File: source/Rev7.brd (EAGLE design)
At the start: 17.4 x 19 mm, 8 parts

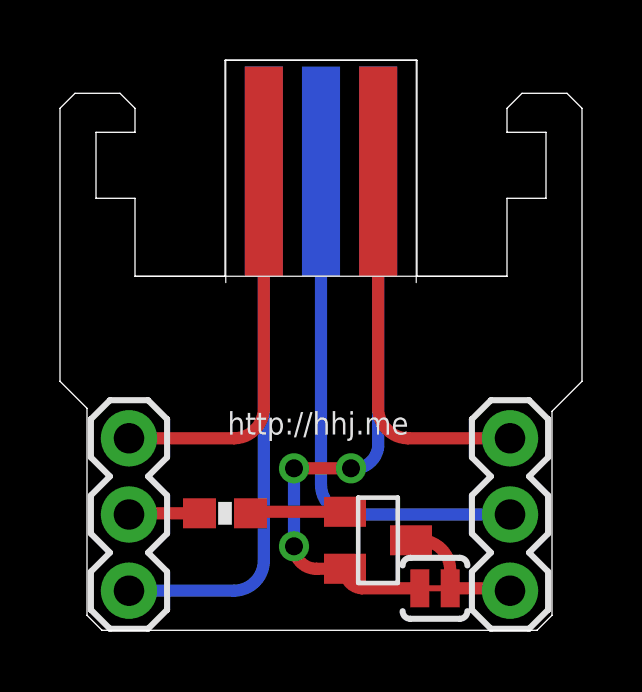
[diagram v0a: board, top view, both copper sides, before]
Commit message: Updated Rev7: down to 1 via and much better signal layout. Pin layout has changed
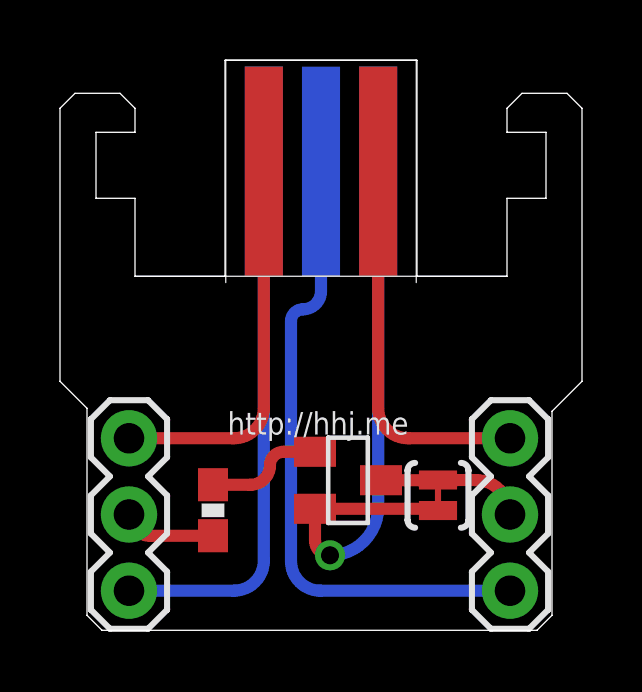
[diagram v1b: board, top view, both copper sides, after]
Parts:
- moved SJ1 3.10 mm to (12.1, 4.50), turned to 90 degrees
- moved Q1 2.24 mm to (9.10, 5.00)
- moved R1 0.41 mm to (4.60, 4.00), turned to 90 degrees
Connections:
- removed net PRES: JP2.2, U$1.PRESENCE
- new net N$2: JP2.3, U$1.PRESENCE
- net N$6: now also JP2.2; no longer JP2.3
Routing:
- net N$2: track 0.00 -> 21.1 mm
- net PRES: track 17.2 -> 0.00 mm
- net EN: track 2.37 -> 3.09 mm
- net N$1: track 3.17 -> 3.86 mm
- net SDA: track 19.7 -> 19.3 mm, vias 3 -> 1
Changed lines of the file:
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@@
 <text x="3.1" y="6.3" size="1.27" layer="22" font="vector" ratio="16" rot="MR180" align="center-left">CLK</text>
 <text x="13.4" y="6.3" size="1.27" layer="22" font="vector" ratio="16" rot="MR0" align="center-left">GND</text>
-<text x="13.2" y="1.3" size="1.27" layer="22" font="vector" ratio="16" rot="MR180" align="center-right">DATA</text>
-<text x="13.2" y="3.8" size="1.27" layer="22" font="vector" ratio="16" rot="MR180" align="center-right">PRES</text>
+<text x="13.2" y="3.8" size="1.27" layer="22" font="vector" ratio="16" rot="MR180" align="center-right">DATA</text>
+<text x="13.2" y="1.3" size="1.27" layer="22" font="vector" ratio="16" rot="MR180" align="center-right">PRES</text>
 <text x="3.1" y="1.3" size="1.27" layer="22" font="vector" ratio="16" rot="MR0" align="center-right">3.3V</text>
 <text x="3.1" y="3.8" size="1.27" layer="22" font="vector" ratio="16" rot="MR180" align="center-left">EN</text>
@@
 <attribute name="VALUE" x="11.325" y="7.67" size="1.27" layer="27" rot="R270"/>
 </element>
-<element name="SJ1" library="SparkFun-Passives" package="SJ_2S-TRACE" value="NC" x="12" y="1.4" smashed="yes"/>
-<element name="Q1" library="SparkFun-DiscreteSemi" package="SOT23" value="" x="10.1" y="3" smashed="yes" rot="R270">
-<attribute name="VALUE" x="9.9095" y="4.016" size="0.4064" layer="27" rot="R270"/>
-</element>
-<element name="R1" library="SparkFun-Resistors" package="0603-RES" value="" x="5" y="3.9" smashed="yes">
-<attribute name="VALUE" x="3.984" y="2.757" size="0.4064" layer="27" font="vector"/>
+<element name="SJ1" library="SparkFun-Passives" package="SJ_2S-TRACE" value="NC" x="12.1" y="4.5" smashed="yes" rot="R90"/>
+<element name="Q1" library="SparkFun-DiscreteSemi" package="SOT23" value="" x="9.1" y="5" smashed="yes" rot="R270">
+<attribute name="VALUE" x="8.9095" y="6.016" size="0.4064" layer="27" rot="R270"/>
+</element>
+<element name="R1" library="SparkFun-Resistors" package="0603-RES" value="" x="4.6" y="4" smashed="yes" rot="R90">
+<attribute name="VALUE" x="5.743" y="2.984" size="0.4064" layer="27" font="vector" rot="R90"/>
 </element>
 <element name="LOGO1" library="SparkFun-Aesthetics" package="OSHW-LOGO-S" value="OSHW-LOGOS" x="14.9" y="9.8" rot="MR0"/>
@@
 </elements>
 <signals>
-<signal name="PRES">
-<contactref element="U$1" pad="PRESENCE"/>
-<contactref element="JP2" pad="2"/>
-<wire x1="8.2" y1="15.3" x2="8.2" y2="4.86" width="0.4064" layer="16"/>
-<wire x1="8.2" y1="4.86" x2="9.2" y2="3.86" width="0.4064" layer="16" curve="90"/>
-<wire x1="9.2" y1="3.86" x2="14.5" y2="3.86" width="0.4064" layer="16"/>
-</signal>
 <signal name="SCL">
 <contactref element="U$1" pad="CLK"/>
@@
 <contactref element="JP1" pad="2"/>
 <contactref element="R1" pad="1"/>
-<wire x1="4.15" y1="3.9" x2="1.84" y2="3.9" width="0.4064" layer="1"/>
-<wire x1="1.84" y1="3.9" x2="1.8" y2="3.86" width="0.4064" layer="1" curve="90"/>
+<wire x1="4.6" y1="3.15" x2="2.51" y2="3.15" width="0.4064" layer="1"/>
+<wire x1="2.51" y1="3.15" x2="1.8" y2="3.86" width="0.4064" layer="1" curve="-90"/>
 </signal>
 <signal name="3.3V">
@@
 <contactref element="SJ1" pad="1"/>
 <contactref element="Q1" pad="2"/>
-<wire x1="11.492" y1="1.4" x2="9.55" y2="1.4" width="0.4064" layer="1"/>
-<wire x1="9.55" y1="1.4" x2="9" y2="2.05" width="0.4064" layer="1" curve="-90"/>
-<wire x1="10.105" y1="15.3" x2="10.105" y2="6.105" width="0.4064" layer="16"/>
-<wire x1="10.105" y1="6.105" x2="9.2" y2="5.4" width="0.4064" layer="16" curve="-90"/>
-<via x="9.2" y="5.4" extent="1-16" drill="0.6"/>
-<wire x1="9.1" y1="2.05" x2="9" y2="2.05" width="0.4064" layer="1"/>
-<via x="7.3" y="5.4" extent="1-16" drill="0.6"/>
-<wire x1="7.3" y1="5.4" x2="7.3" y2="2.8" width="0.4064" layer="16"/>
-<via x="7.3" y="2.8" extent="1-16" drill="0.6"/>
-<wire x1="7.3" y1="2.8" x2="8.05" y2="2.05" width="0.4064" layer="1" curve="90"/>
-<wire x1="8.05" y1="2.05" x2="9" y2="2.05" width="0.4064" layer="1"/>
-<wire x1="7.3" y1="5.4" x2="9.2" y2="5.4" width="0.4064" layer="1"/>
+<wire x1="10.105" y1="15.3" x2="10.105" y2="4.105" width="0.4064" layer="16"/>
+<wire x1="10.105" y1="4.105" x2="8.5" y2="2.5" width="0.4064" layer="16" curve="-90"/>
+<via x="8.5" y="2.5" extent="1-16" drill="0.6"/>
+<wire x1="8" y1="4.05" x2="12.042" y2="4.05" width="0.4064" layer="1"/>
+<wire x1="12.042" y1="4.05" x2="12.1" y2="3.992" width="0.4064" layer="1" curve="-90"/>
+<wire x1="8" y1="4.05" x2="8" y2="3" width="0.4064" layer="1"/>
+<wire x1="8" y1="3" x2="8.5" y2="2.5" width="0.4064" layer="1" curve="90"/>
 </signal>
 <signal name="N$1">
 <contactref element="Q1" pad="1"/>
 <contactref element="R1" pad="2"/>
-<wire x1="5.85" y1="3.9" x2="5.9" y2="3.95" width="0.4064" layer="1" curve="-90"/>
-<wire x1="5.9" y1="3.95" x2="9" y2="3.95" width="0.4064" layer="1"/>
+<wire x1="8" y1="5.95" x2="6.95" y2="5.95" width="0.4064" layer="1"/>
+<wire x1="6.95" y1="5.95" x2="6.5" y2="5.5" width="0.4064" layer="1" curve="90"/>
+<wire x1="6.5" y1="5.5" x2="5.85" y2="4.85" width="0.4064" layer="1" curve="-90"/>
+<wire x1="5.85" y1="4.85" x2="4.6" y2="4.85" width="0.4064" layer="1"/>
 </signal>
 <signal name="GND">
@@
 <contactref element="SJ1" pad="2"/>
 <contactref element="Q1" pad="3"/>
+<wire x1="10.2" y1="5" x2="12.092" y2="5" width="0.4064" layer="1"/>
+<wire x1="12.092" y1="5" x2="12.1" y2="5.008" width="0.4064" layer="1" curve="90"/>
+<contactref element="JP2" pad="2"/>
+<wire x1="12.1" y1="5.008" x2="13.352" y2="5.008" width="0.4064" layer="1"/>
+<wire x1="13.352" y1="5.008" x2="14.5" y2="3.86" width="0.4064" layer="1" curve="-90"/>
+</signal>
+<signal name="N$2">
+<contactref element="U$1" pad="PRESENCE"/>
 <contactref element="JP2" pad="3"/>
-<wire x1="12.508" y1="1.4" x2="14.42" y2="1.4" width="0.4064" layer="1"/>
-<wire x1="14.42" y1="1.4" x2="14.5" y2="1.32" width="0.4064" layer="1" curve="-90"/>
-<wire x1="12.508" y1="1.4" x2="12.508" y2="2" width="0.4064" layer="1"/>
-<wire x1="12.508" y1="2" x2="11.508" y2="3" width="0.4064" layer="1" curve="90"/>
-<wire x1="11.508" y1="3" x2="11.2" y2="3" width="0.4064" layer="1"/>
+<wire x1="8.2" y1="15.3" x2="8.2" y2="11.3" width="0.4064" layer="16"/>
+<wire x1="8.2" y1="11.3" x2="7.6" y2="10.7" width="0.4064" layer="16" curve="-90"/>
+<wire x1="7.6" y1="10.7" x2="7.2" y2="10.3" width="0.4064" layer="16" curve="90"/>
+<wire x1="7.2" y1="10.3" x2="7.2" y2="2.3" width="0.4064" layer="16"/>
+<wire x1="7.2" y1="2.3" x2="8.18" y2="1.32" width="0.4064" layer="16" curve="90"/>
+<wire x1="8.18" y1="1.32" x2="14.5" y2="1.32" width="0.4064" layer="16"/>
 </signal>
 </signals>
